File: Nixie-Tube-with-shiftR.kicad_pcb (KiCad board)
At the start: 2 copper layers, 37 x 56.3 mm, 60 parts, among them J1 Conn_01x06_Male, J2 HV_IN, J3 Conn_01x06_Female, J4 HV_OUT, Q1 MMBTA42LT1, Q10 MMBTA42LT1, Q11 AO3400, Q12 AO3400, Q13 AO3400, Q14 MMBTA42LT1, Q15 MMBTA42LT1, Q2 MMBTA42LT1, Q3 MMBTA42LT1, Q4 MMBTA42LT1, Q5 MMBTA42LT1, Q6 MMBTA42LT1, Q7 MMBTA42LT1, Q8 MMBTA42LT1, Q9 MMBTA42LT1, U1 74HC595D, U2 nixie-tube-qs27, U3 74HC595D, U4 ams1117-5.0

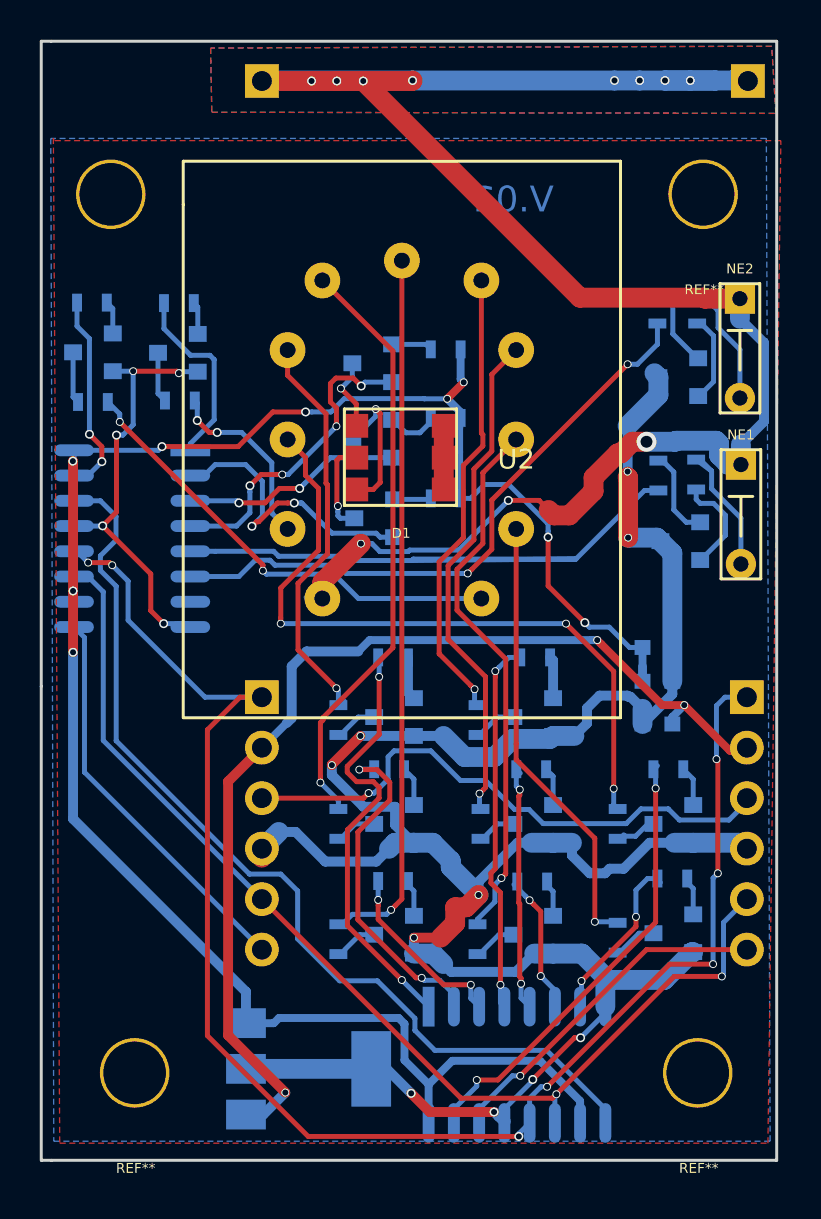
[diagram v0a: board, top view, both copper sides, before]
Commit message: changed AO3400 pin position (2 board)
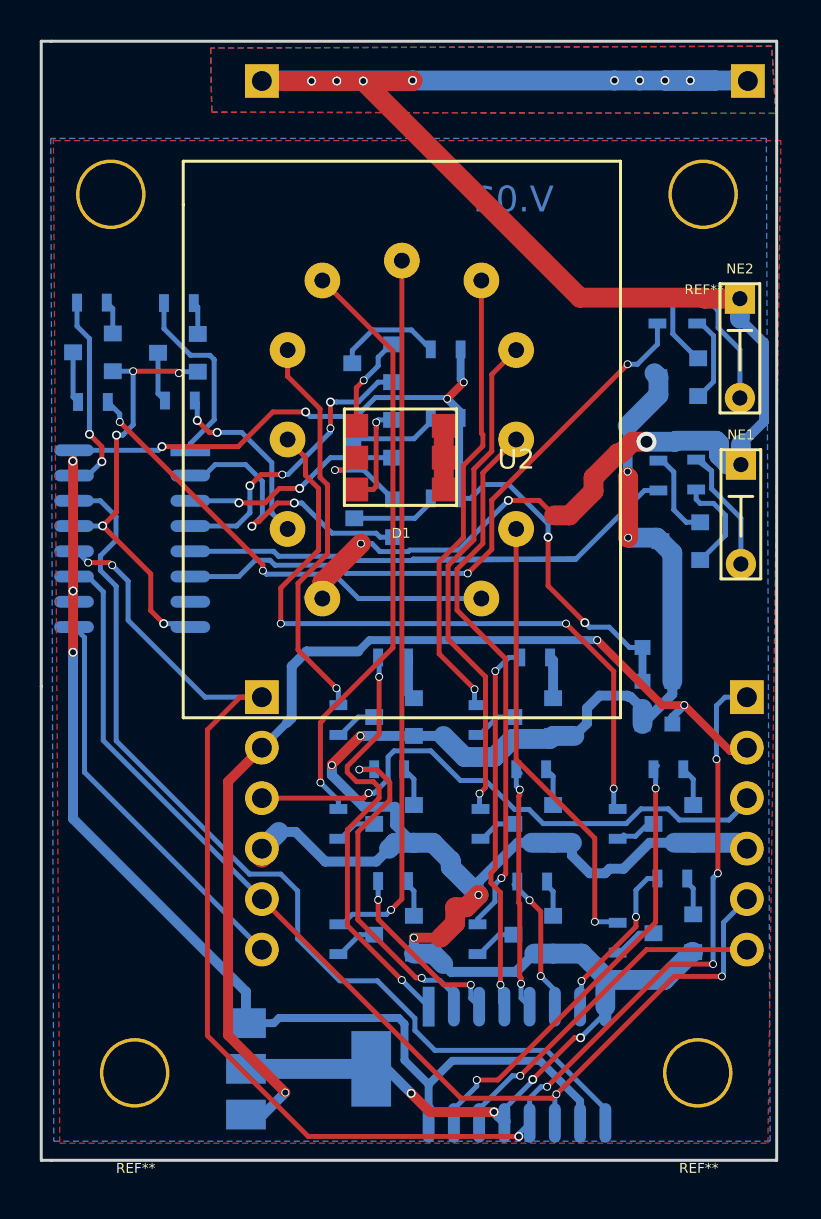
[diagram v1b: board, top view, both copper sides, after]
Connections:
- Q11 pad 1: Net-(Q11-Pad1) -> Net-(D1-Pad2)
- Q11 pad 3: Net-(D1-Pad2) -> Net-(Q11-Pad3)
- Q12 pad 1: Net-(Q12-Pad1) -> Net-(D1-Pad3)
- Q12 pad 3: Net-(D1-Pad3) -> Net-(Q12-Pad3)
- Q13 pad 1: Net-(Q13-Pad1) -> Net-(D1-Pad4)
- Q13 pad 3: Net-(D1-Pad4) -> Net-(Q13-Pad3)
- R11 pad 2: Net-(Q11-Pad1) -> Net-(Q11-Pad3)
- R12 pad 2: Net-(Q12-Pad1) -> Net-(Q12-Pad3)
- R13 pad 2: Net-(Q13-Pad1) -> Net-(Q13-Pad3)
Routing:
- net Net-(Q13-Pad3): track 0.00 -> 5.43 mm
- net Net-(Q12-Pad3): track 0.00 -> 4.55 mm
- net Net-(Q11-Pad3): track 0.00 -> 4.45 mm
- net Net-(Q12-Pad1): track 2.65 -> 0.00 mm
- net Net-(Q13-Pad1): track 2.05 -> 0.00 mm
- net Net-(D1-Pad3): track 7.14 -> 5.20 mm
- net Net-(Q11-Pad1): track 1.87 -> 0.00 mm
- net Net-(D1-Pad4): track 3.71 -> 4.87 mm
- net /Blue: track 16.1 -> 15.0 mm
- net +5V: track 102.7 -> 101.6 mm

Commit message: remove silkscreen on female pins, re routed some of the tracks
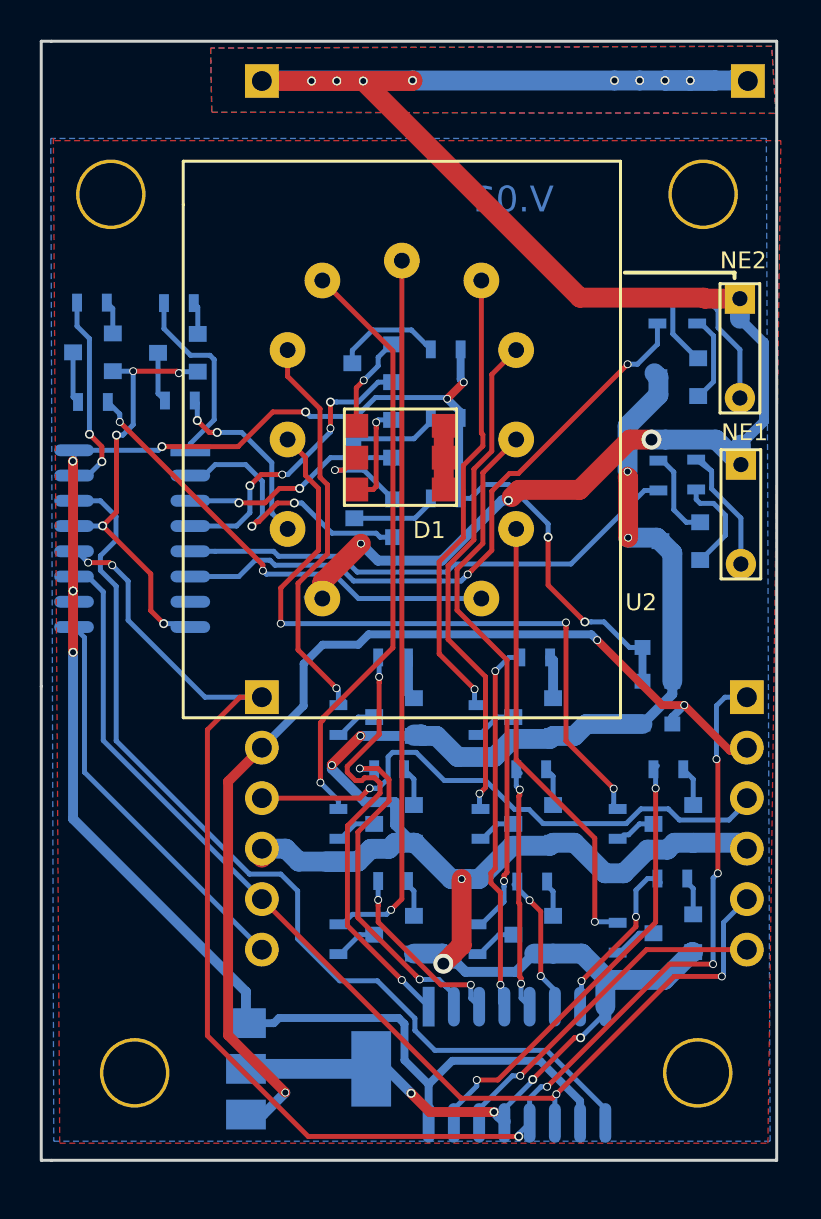
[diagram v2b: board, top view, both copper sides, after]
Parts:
- J2: footprint Socket_Strips:Socket_Strip_Angled_1x01_Pitch2.54mm -> nixie-tube-fp:Socket_Strip_Angled_1x01_Pitch2.54mm_without_silk
- J3: footprint Socket_Strips:Socket_Strip_Angled_1x06_Pitch2.54mm -> nixie-tube-fp:Socket_Strip_Angled_1x06_Pitch2.54mm_without_silk
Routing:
- net /DotU: track 33.5 -> 25.7 mm
- net GND: track 149.0 -> 147.1 mm
- net Net-(J2-Pad1): track 95.1 -> 93.8 mm
- net /DotD: track 31.5 -> 32.1 mm

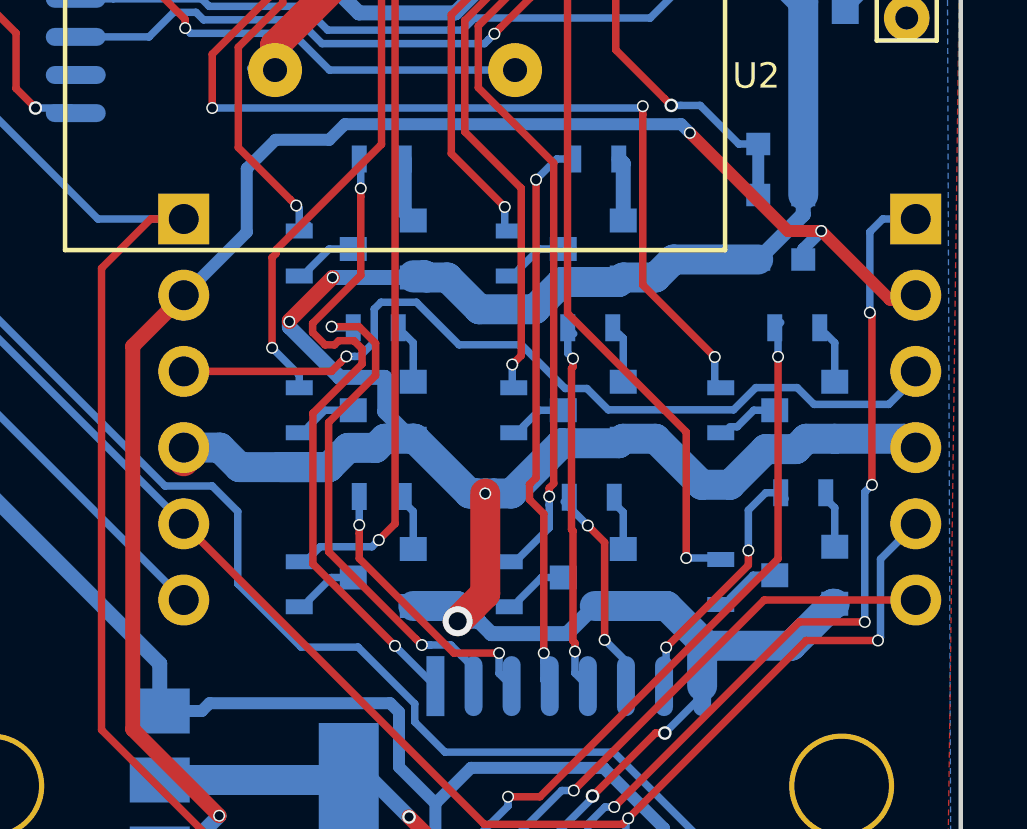
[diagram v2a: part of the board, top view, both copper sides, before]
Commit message: fixed some badly routed tracks
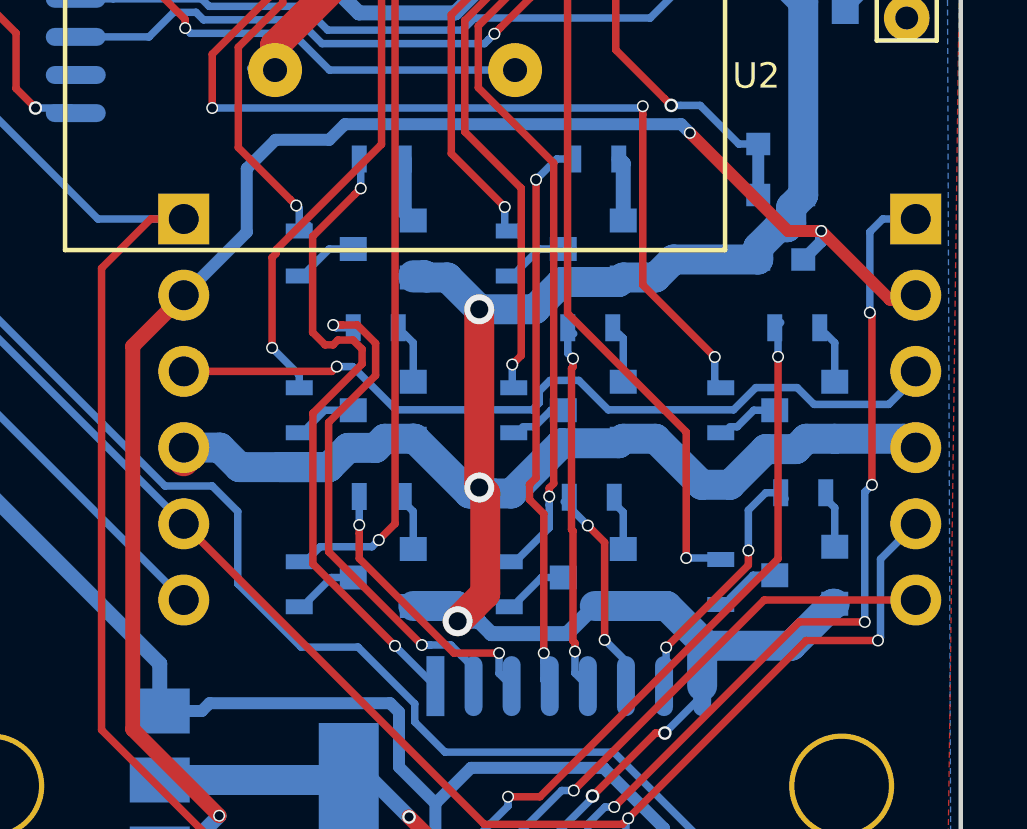
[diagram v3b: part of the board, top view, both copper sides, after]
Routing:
- net GND: track 147.1 -> 142.3 mm, vias 15 -> 14
- net /PWREN: track 28.5 -> 27.1 mm

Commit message: finalized every component and generated gerber file
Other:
- board text added: "GND"
- board text added: "MISO"
- board text added: "MOSI"
- board text added: "PWREN"
- board text added: "SCK"
- board text added: "STORE"
- board text added: "VDC"
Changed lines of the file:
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@@
     (links 108)
     (no_connects 0)
-    (area 151.424999 40.224999 188.575001 96.675001)
+    (area 141.050001 39.055 208.899524 100.700001)
     (thickness 1.6)
-    (drawings 15)
+    (drawings 22)
     (tracks 781)
     (zones 0)
@@
     (visible_elements 7FFEFFFF)
     (pcbplotparams
-      (layerselection 0x0d4fc_80000001)
+      (layerselection 0x0d0fc_80000001)
       (usegerberextensions true)
       (usegerberattributes true)
@@
     (fp_line (start -10.55 -14.5) (end -10.55 1.8) (layer B.CrtYd) (width 0.05))
     (fp_line (start -10.55 1.8) (end 1.8 1.8) (layer B.CrtYd) (width 0.05))
-    (fp_text user %R (at -4.38 2.27 180) (layer B.Fab)
+    (fp_text user %R (at 0.27 3.77 180) (layer B.Fab)
       (effects (font (size 1 1) (thickness 0.15)) (justify mirror))
     )
@@
     )
   )
+  (gr_text MISO (at 166.79 86.12) (layer F.SilkS)
+    (effects (font (size 1.5 1.5) (thickness 0.3)))
+  )
+  (gr_text MOSI (at 182.72 86.46) (layer F.SilkS)
+    (effects (font (size 1.5 1.5) (thickness 0.3)))
+  )
+  (gr_text SCK (at 174.86 83.75) (layer F.SilkS)
+    (effects (font (size 1.5 1.5) (thickness 0.3)))
+  )
+  (gr_text GND (at 174.67 81.17) (layer F.SilkS)
+    (effects (font (size 1.5 1.5) (thickness 0.3)))
+  )
+  (gr_text PWREN (at 175.05 78.65) (layer F.SilkS)
+    (effects (font (size 1.5 1.5) (thickness 0.3)))
+  )
+  (gr_text VDC (at 174.01 76.03) (layer F.SilkS)
+    (effects (font (size 1.5 1.5) (thickness 0.3)))
+  )
+  (gr_text STORE (at 174.35 73.27) (layer F.SilkS)
+    (effects (font (size 1.5 1.5) (thickness 0.3)))
+  )
   (gr_line (start 184.56 51.94) (end 184.56 52.26) (layer B.SilkS) (width 0.2))

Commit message: finalized tracks and added symbols
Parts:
- moved R4 0.17 mm to (173.4, 85.3)
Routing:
- net GND: track 142.3 -> 178.5 mm, vias 14 -> 18
- net +5V: track 101.6 -> 126.7 mm, vias 9 -> 10
- net Net-(R2-Pad1): track 23.5 -> 31.1 mm, vias 2 -> 0
- net /Blue: track 15.0 -> 18.3 mm, vias 4 -> 0
- net /s9: track 9.52 -> 12.2 mm
- net +VDC: track 53.6 -> 55.6 mm
- net /s1: track 22.1 -> 20.3 mm
- net /s2: track 17.2 -> 15.6 mm
- net Net-(R8-Pad1): track 29.9 -> 31.3 mm
- net Net-(R10-Pad1): track 35.5 -> 36.8 mm, vias 3 -> 5
- net Net-(J2-Pad1): track 93.8 -> 92.9 mm, vias 11 -> 10
- net Net-(R4-Pad1): track 27.4 -> 28.1 mm
- net Net-(R3-Pad1): track 22.6 -> 23.3 mm
- net /STORE: track 80.0 -> 80.7 mm
- net /DotD: track 32.1 -> 32.7 mm
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
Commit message: finalized everything and ready to send out
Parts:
- added Z?: lightning, nixie-tube-fp:lightning, F.Cu at (181.7, 42.5)
- added Z?: skull, nixie-tube-fp:skull, F.Cu at (168.9, 42.9)
- added Z?: skull, nixie-tube-fp:skull, B.Cu at (168.8, 42.9)
- added Z?: lightning, nixie-tube-fp:lightning, B.Cu at (181.7, 42.5)
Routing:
- net Net-(J2-Pad1): track 92.9 -> 98.5 mm
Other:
- board text added: "HV"

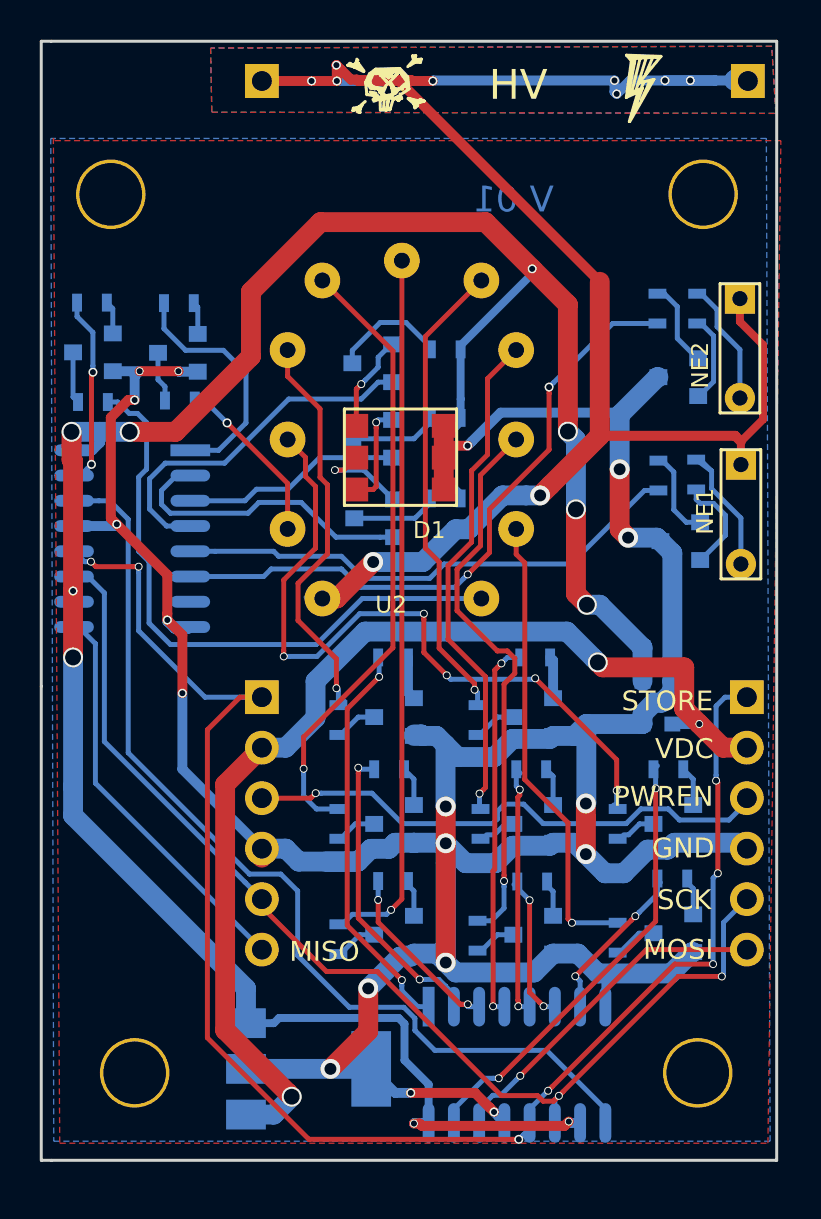
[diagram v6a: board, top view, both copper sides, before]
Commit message: fixed various bugs
RGB led not connected properly to the mosfet
AO3400 pin orientation is not same with datasheet
move silkscreen away on neon footprint
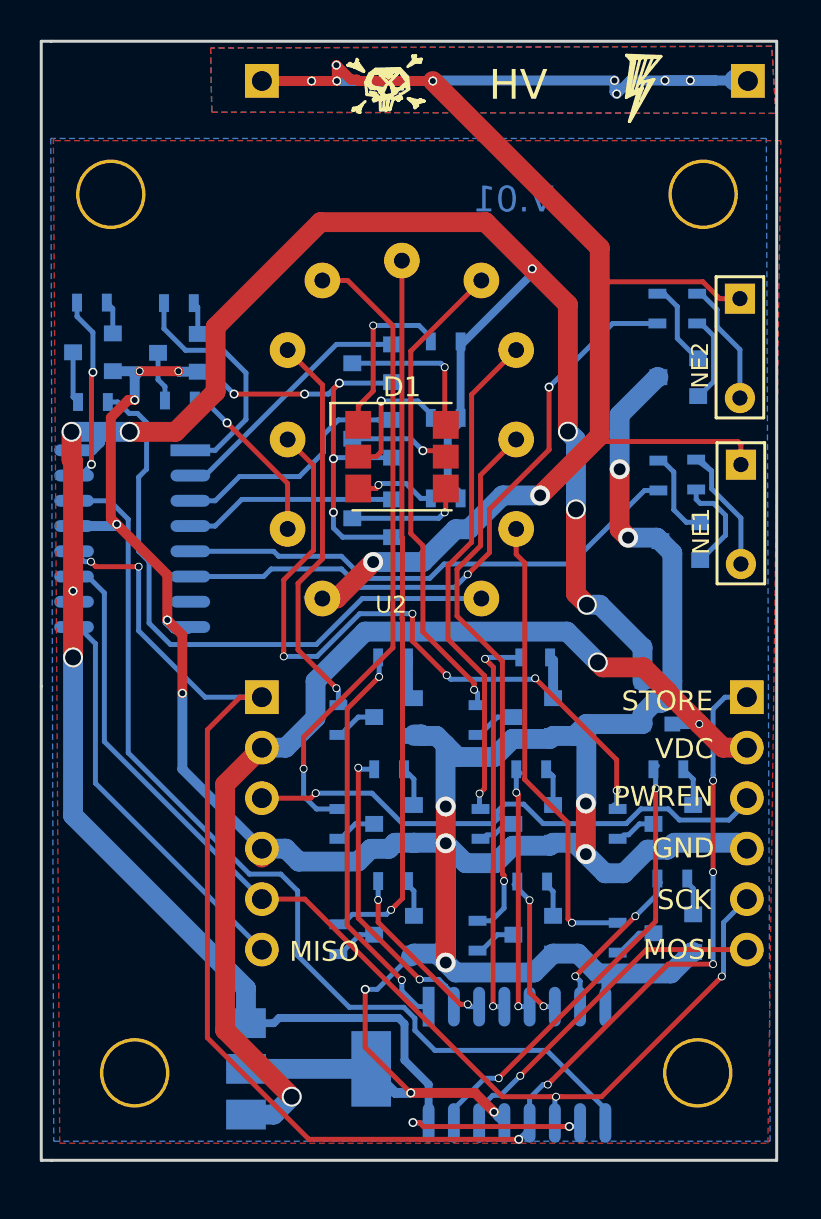
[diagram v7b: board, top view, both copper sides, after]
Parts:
- D1: value LED_CRGB -> LED_RGB_BGR; footprint nixie-tube-fp:Rgb-Led -> nixie-tube-fp:LED_RGB_5050-6
- moved R11 7.90 mm to (171.8, 55.4)
- moved Q11 7.80 mm to (168.2, 56.5)
- moved Q13 7.80 mm to (168.2, 64.3)
- moved R13 7.50 mm to (171.8, 63.3)
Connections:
- D1 pad 1: GND -> Net-(D1-Pad1)
- Q11 pad 1: Net-(D1-Pad2) -> /Red
- Q11 pad 2: /Red -> GND
- Q11 pad 3: Net-(Q11-Pad3) -> Net-(D1-Pad6)
- Q12 pad 1: Net-(D1-Pad3) -> /Green
- Q12 pad 2: /Green -> GND
- Q12 pad 3: Net-(Q12-Pad3) -> Net-(D1-Pad5)
- Q13 pad 1: Net-(D1-Pad4) -> /Blue
- Q13 pad 2: /Blue -> GND
- Q13 pad 3: Net-(Q13-Pad3) -> Net-(D1-Pad4)
- R11 pad 2: Net-(Q11-Pad3) -> Net-(D1-Pad1)
- R12 pad 2: Net-(Q12-Pad3) -> Net-(D1-Pad2)
- R13 pad 2: Net-(Q13-Pad3) -> Net-(D1-Pad3)
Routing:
- net GND: track 178.5 -> 188.9 mm, vias 18 -> 21
- net Net-(D1-Pad1): track 0.00 -> 9.15 mm, vias 0 -> 1
- net Net-(D1-Pad6): track 0.00 -> 7.65 mm, vias 0 -> 1
- net /Blue: track 18.3 -> 10.8 mm
- net Net-(Q13-Pad3): track 5.80 -> 0.00 mm
- net Net-(J2-Pad1): track 98.5 -> 92.7 mm
- net Net-(D1-Pad5): track 0.00 -> 5.12 mm, vias 0 -> 1
- net Net-(Q12-Pad3): track 4.55 -> 0.00 mm
- net Net-(Q11-Pad3): track 4.45 -> 0.00 mm
- net Net-(D1-Pad2): track 4.92 -> 7.32 mm
- net /Green: track 11.0 -> 13.1 mm
- net /Red: track 15.3 -> 13.6 mm
- net +VDC: track 55.6 -> 54.4 mm
- net Net-(D1-Pad4): track 4.87 -> 5.99 mm
- net /s4: track 19.1 -> 20.0 mm
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
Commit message: added few things
lightning symbol on neon and around nixie tube
via stiching
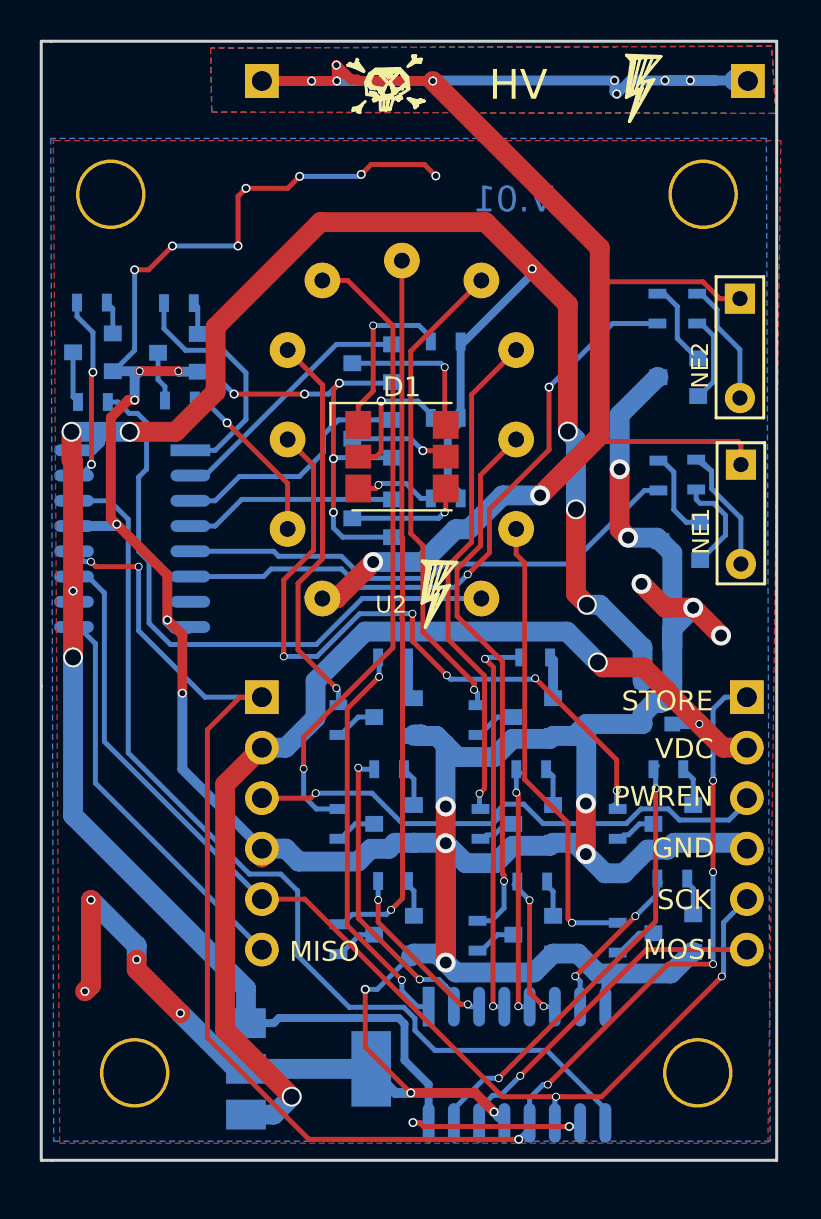
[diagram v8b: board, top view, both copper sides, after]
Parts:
- added Z?: lightning, nixie-tube-fp:lightning, B.Cu at (186.8, 64.1)
- added Z?: lightning, nixie-tube-fp:lightning, B.Cu at (186.7, 55.8)
- added Z?: lightning, nixie-tube-fp:lightning, F.Cu at (171.4, 68.0)
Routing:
- net GND: track 188.9 -> 237.8 mm, vias 21 -> 35
